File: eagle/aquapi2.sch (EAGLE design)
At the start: 5 parts, among them IC1 RASPBERRY_PI_ZERO_W__V1.3_

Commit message: schemtic added
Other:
- moved on the sheet: PH_PROBE
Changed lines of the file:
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@@
 </instance>
 <instance part="U$2" gate="G$1" x="200.66" y="48.26" smashed="yes"/>
-<instance part="PH_PROBE" gate="A" x="12.7" y="35.56" smashed="yes" rot="R90">
-<attribute name="NAME" x="6.985" y="29.21" size="1.778" layer="95" rot="R90"/>
-<attribute name="VALUE" x="20.32" y="29.21" size="1.778" layer="96" rot="R90"/>
+<instance part="PH_PROBE" gate="A" x="-12.7" y="40.64" smashed="yes" rot="R90">
+<attribute name="NAME" x="-18.415" y="34.29" size="1.778" layer="95" rot="R90"/>
+<attribute name="VALUE" x="-5.08" y="34.29" size="1.778" layer="96" rot="R90"/>
 </instance>
 <instance part="SUPPLY1" gate="GND" x="33.02" y="35.56" smashed="yes">
 <attribute name="VALUE" x="31.115" y="32.385" size="1.778" layer="96"/>
 </instance>
-<instance part="SUPPLY2" gate="GND" x="17.78" y="20.32" smashed="yes">
-<attribute name="VALUE" x="15.875" y="17.145" size="1.778" layer="96"/>
+<instance part="SUPPLY2" gate="GND" x="-7.62" y="25.4" smashed="yes">
+<attribute name="VALUE" x="-9.525" y="22.225" size="1.778" layer="96"/>
 </instance>
 <instance part="SUPPLY3" gate="GND" x="246.38" y="63.5" smashed="yes">
@@
 <attribute name="VALUE" x="168.275" y="55.245" size="1.778" layer="96"/>
 </instance>
-<instance part="SUPPLY6" gate="+5V" x="12.7" y="12.7" smashed="yes" rot="R180">
-<attribute name="VALUE" x="14.605" y="9.525" size="1.778" layer="96" rot="R180"/>
+<instance part="SUPPLY6" gate="+5V" x="-12.7" y="17.78" smashed="yes" rot="R180">
+<attribute name="VALUE" x="-10.795" y="14.605" size="1.778" layer="96" rot="R180"/>
 </instance>
 <instance part="SUPPLY7" gate="+5V" x="33.02" y="81.28" smashed="yes" rot="R180">
@@
 <attribute name="VALUE" x="31.115" y="47.625" size="1.778" layer="96"/>
 </instance>
-<instance part="U$3" gate="G$1" x="106.68" y="-71.12" smashed="yes"/>
-<instance part="SUPPLY14" gate="GND" x="93.98" y="-35.56" smashed="yes">
-<attribute name="VALUE" x="92.075" y="-38.735" size="1.778" layer="96"/>
+<instance part="U$3" gate="G$1" x="66.04" y="-55.88" smashed="yes"/>
+<instance part="SUPPLY14" gate="GND" x="53.34" y="-20.32" smashed="yes">
+<attribute name="VALUE" x="51.435" y="-23.495" size="1.778" layer="96"/>
 </instance>
-<instance part="SUPPLY15" gate="+5V" x="93.98" y="-20.32" smashed="yes" rot="R180">
-<attribute name="VALUE" x="95.885" y="-23.495" size="1.778" layer="96" rot="R180"/>
+<instance part="SUPPLY15" gate="+5V" x="53.34" y="-5.08" smashed="yes" rot="R180">
+<attribute name="VALUE" x="55.245" y="-8.255" size="1.778" layer="96" rot="R180"/>
 </instance>
 </instances>
@@
 <segment>
 <pinref part="PH_PROBE" gate="A" pin="1"/>
-<wire x1="10.16" y1="33.02" x2="10.16" y2="22.86" width="0.1524" layer="91"/>
-<junction x="10.16" y="22.86"/>
-<label x="7.62" y="22.86" size="1.778" layer="95" rot="R270"/>
+<wire x1="-15.24" y1="38.1" x2="-15.24" y2="27.94" width="0.1524" layer="91"/>
+<junction x="-15.24" y="27.94"/>
+<label x="-17.78" y="27.94" size="1.778" layer="95" rot="R270"/>
 </segment>
 <segment>
@@
 <segment>
 <pinref part="PH_PROBE" gate="A" pin="3"/>
-<wire x1="15.24" y1="33.02" x2="15.24" y2="22.86" width="0.1524" layer="91"/>
-<label x="17.78" y="22.86" size="1.778" layer="95"/>
-<junction x="15.24" y="22.86"/>
+<wire x1="-10.16" y1="38.1" x2="-10.16" y2="27.94" width="0.1524" layer="91"/>
+<label x="-7.62" y="27.94" size="1.778" layer="95"/>
+<junction x="-10.16" y="27.94"/>
 <pinref part="SUPPLY2" gate="GND" pin="GND"/>
-<wire x1="15.24" y1="22.86" x2="17.78" y2="22.86" width="0.1524" layer="91"/>
-<junction x="17.78" y="22.86"/>
+<wire x1="-10.16" y1="27.94" x2="-7.62" y2="27.94" width="0.1524" layer="91"/>
+<junction x="-7.62" y="27.94"/>
 </segment>
 <segment>
@@
 <segment>
 <pinref part="U$3" gate="G$1" pin="GND"/>
-<wire x1="95.25" y1="-30.48" x2="93.98" y2="-30.48" width="0.1524" layer="91"/>
+<wire x1="54.61" y1="-15.24" x2="53.34" y2="-15.24" width="0.1524" layer="91"/>
 <pinref part="SUPPLY14" gate="GND" pin="GND"/>
-<wire x1="93.98" y1="-30.48" x2="93.98" y2="-33.02" width="0.1524" layer="91"/>
+<wire x1="53.34" y1="-15.24" x2="53.34" y2="-17.78" width="0.1524" layer="91"/>
 </segment>
 </net>
@@
 <segment>
 <pinref part="PH_PROBE" gate="A" pin="2"/>
-<wire x1="12.7" y1="33.02" x2="12.7" y2="22.86" width="0.1524" layer="91"/>
-<junction x="12.7" y="22.86"/>
+<wire x1="-12.7" y1="38.1" x2="-12.7" y2="27.94" width="0.1524" layer="91"/>
+<junction x="-12.7" y="27.94"/>
 <pinref part="SUPPLY6" gate="+5V" pin="+5V"/>
-<wire x1="12.7" y1="22.86" x2="12.7" y2="15.24" width="0.1524" layer="91"/>
+<wire x1="-12.7" y1="27.94" x2="-12.7" y2="20.32" width="0.1524" layer="91"/>
 </segment>
 <segment>
@@
 <pinref part="U$3" gate="G$1" pin="VCC"/>
 <pinref part="SUPPLY15" gate="+5V" pin="+5V"/>
-<wire x1="95.25" y1="-15.24" x2="93.98" y2="-15.24" width="0.1524" layer="91"/>
-<wire x1="93.98" y1="-15.24" x2="93.98" y2="-17.78" width="0.1524" layer="91"/>
+<wire x1="54.61" y1="0" x2="53.34" y2="0" width="0.1524" layer="91"/>
+<wire x1="53.34" y1="0" x2="53.34" y2="-2.54" width="0.1524" layer="91"/>
 </segment>
 </net>

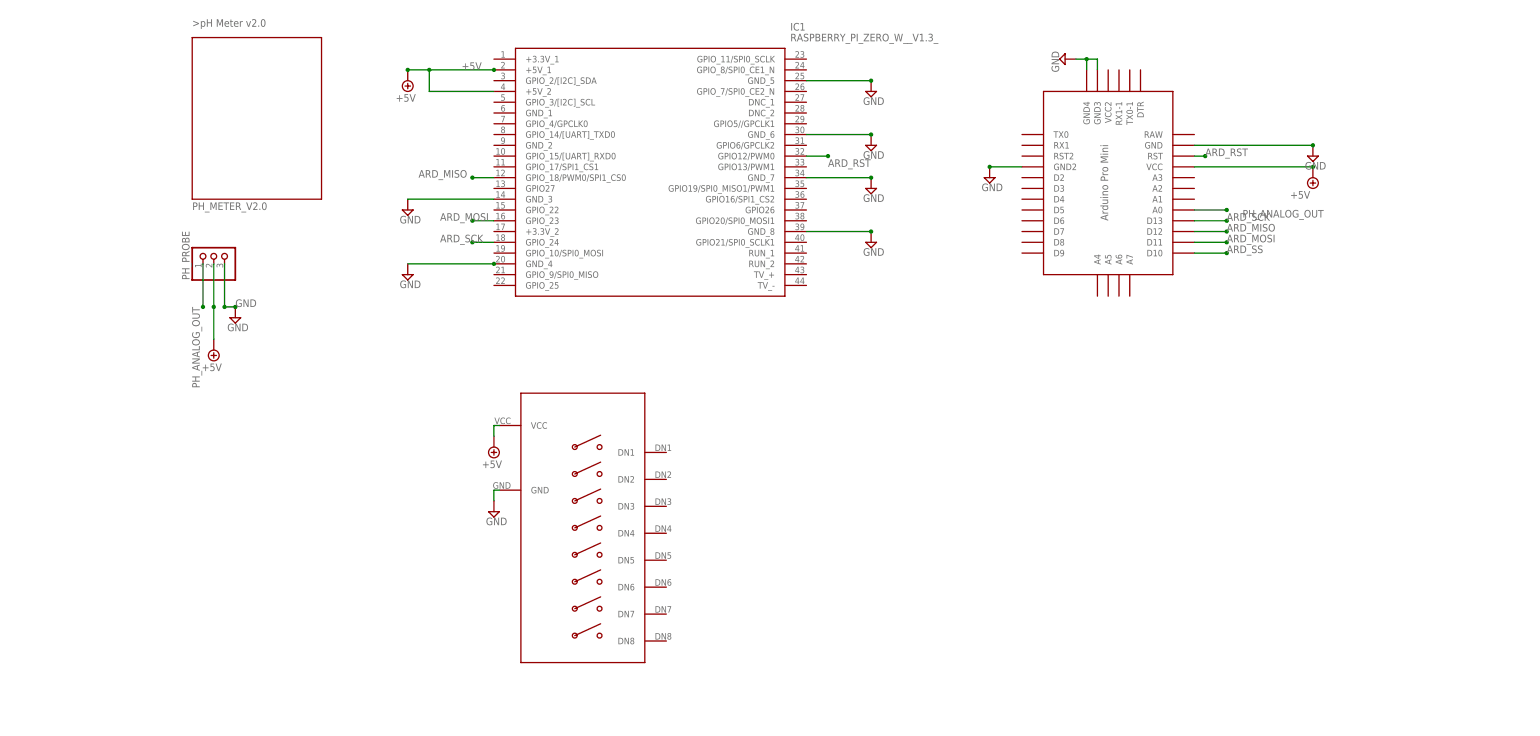
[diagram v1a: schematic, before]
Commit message: arudino device lib fixed
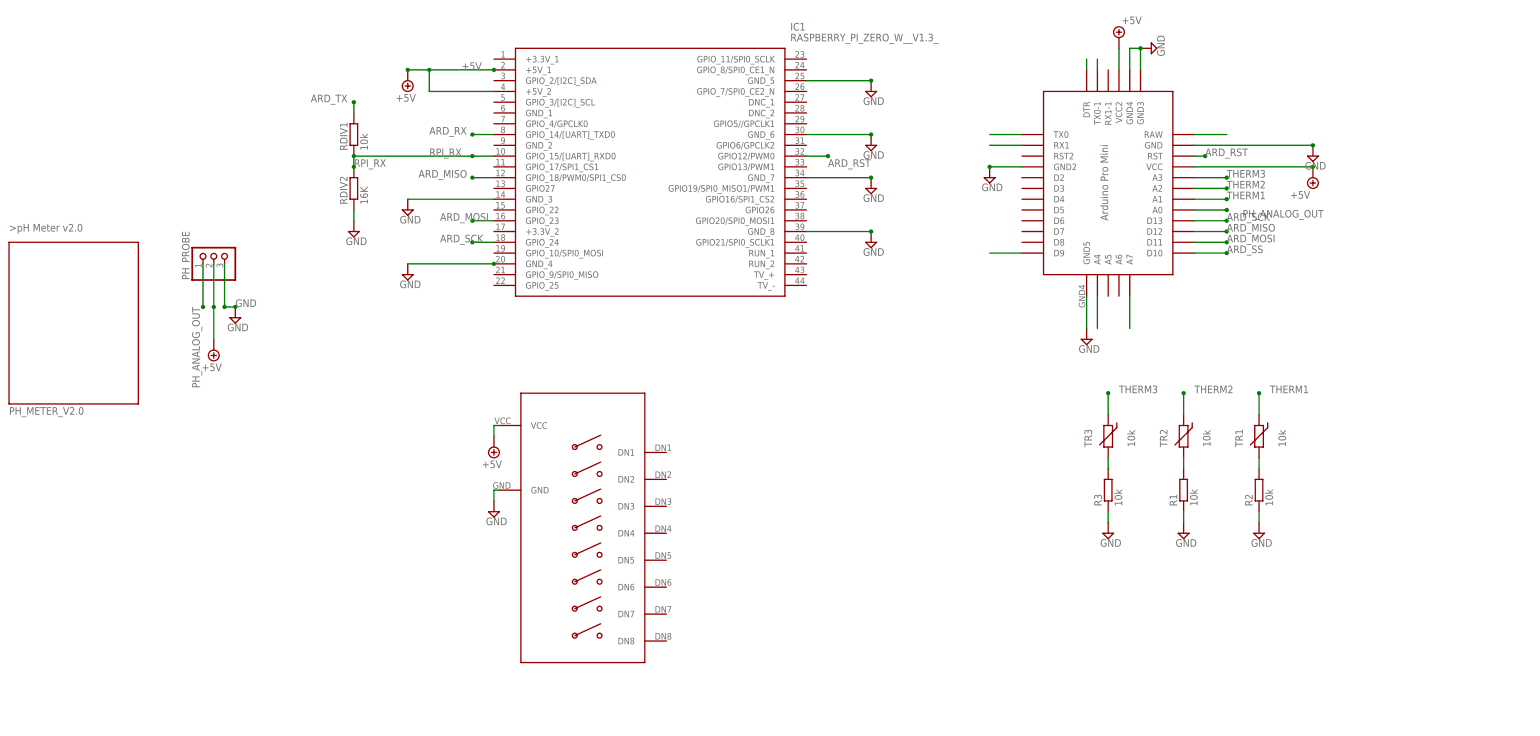
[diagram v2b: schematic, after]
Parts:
- added R1, R2, R3, RDIV1: 10k, rcl:R-EU_R0805
- added RDIV2: 16K, rcl:R-EU_R0805
- added TR1, TR2, TR3: 10k, discrete:THERMISTOR_R-2,5
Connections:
- new net ARD_RX: IC1.GPIO_14/[UART]_TXD0
- new net ARD_TX: RDIV1.2
- new net N$1: R2.2, TR1.2
- new net N$10: U$2.TX0-1
- new net N$13: U$2.GND
- new net N$14: U$2.GND5
- new net N$15: U$2.DTR
- new net N$2: R1.2, TR2.2
- new net N$3: R3.2, TR3.2
- new net N$4: U$2.RAW
- new net N$5: U$2.A7
- new net N$6: U$2.D9
- new net N$7: U$2.A4
- new net N$8: U$2.TX0
- new net N$9: U$2.RX1
- new net RPI_RX: IC1.GPIO_15/[UART]_RXD0, RDIV1.1, RDIV2.2
- new net THERM1: TR1.1, U$2.A1
- new net THERM2: TR2.1, U$2.A2
- new net THERM3: TR3.1, U$2.A3
- net +5V: now also U$2.VCC2
- net GND: now also R1.1, R2.1, R3.1, RDIV2.1; no longer U$2.GND

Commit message: Squashed commit of the following:
commit 7dce77e1b018337bae77b73dfeb2fe2afd6dd7fb
Author: rafal <ravmiecznk@gmail.com>
Date:   Mon Mar 27 18:15:28 2023 +0200

    new constructor from struct

commit 8f6d84a0210c76b2bc0acb519426c939a0a5c33f
Author: rafal <ravmiecznk@gmail.com>
Date:   Mon Mar 27 18:13:10 2023 +0200

    usart draft works

commit a12afc0a744ad612be8265cef467c83d1d3cefab
Author: rafal <ravmiecznk@gmail.com>
Date:   Mon Mar 27 17:49:51 2023 +0200

    schematic fix

commit a0211998f02243aec53f4161e691c0fde81374dd
Author: rafal <ravmiecznk@gmail.com>
Date:   Mon Mar 27 17:49:04 2023 +0200

    Usart constr added

commit c2ed277544ca2c68a412f2a85b5fd8a9273f73a5
Author: rafal <ravmiecznk@gmail.com>
Date:   Sun Mar 26 22:08:04 2023 +0200

    usart and circ buffer added

commit b830d1946cd96a0de6c5bb9a34da8aa961058b17
Author: rafal <ravmiecznk@gmail.com>
Date:   Sun Mar 26 19:27:24 2023 +0200

    avr cpp code added
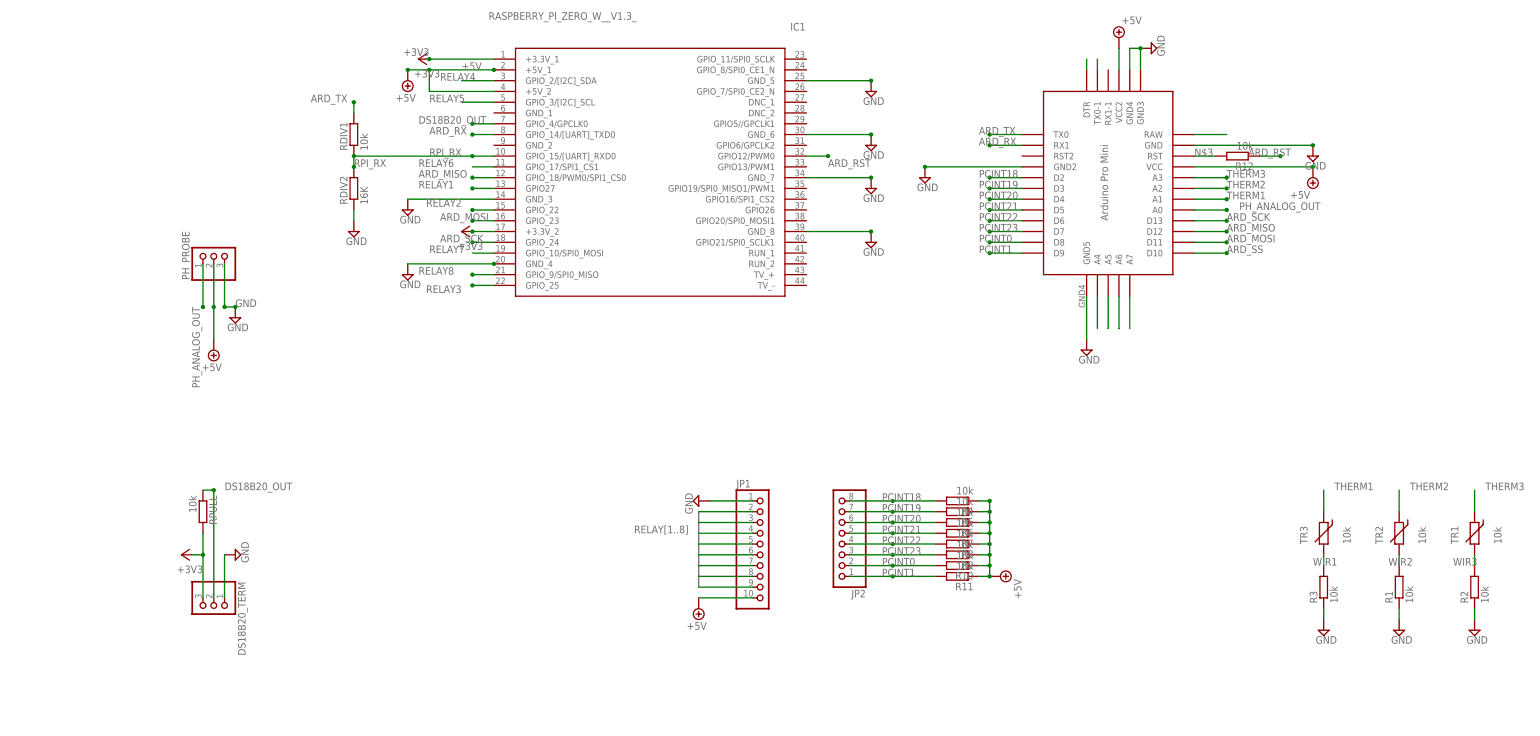
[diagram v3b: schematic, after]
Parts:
- removed U$1: PH_METER_V2.0, dforbot:PH_METER_V2.0
- removed U$3: RELAY_X8, RELAYx8:RELAY_X8
- added DS18B20_TERM: (no value), pinhead:PINHD-1X3
- added JP1: (no value), pinhead:PINHD-1X10
- added JP2: (no value), pinhead:PINHD-1X8
- added R10, R11, R12, R4, R5, R6, R7, R8, R9, RPULL: 10k, rcl:R-EU_R0805
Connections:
- net N$1 renamed WIR3
- net N$2 renamed WIR2
- net N$3 renamed WIR1
- removed net N$14: U$2.GND5
- removed net N$6: U$2.D9
- removed net N$8: U$2.TX0
- removed net N$9: U$2.RX1
- new net +3V3: DS18B20_TERM.3, IC1.+3.3V_1, IC1.+3.3V_2, RPULL.2
- new net DS18B20_OUT: DS18B20_TERM.2, IC1.GPIO_4/GPCLK0, RPULL.1
- new net N$1: U$2.A5
- new net N$2: U$2.A6
- new net N$3: R12.2, U$2.RST
- new net PCINT0: JP2.2, R10.2, U$2.D8
- new net PCINT1: JP2.1, R11.2, U$2.D9
- new net PCINT18: JP2.8, R4.2, U$2.D2
- new net PCINT19: JP2.7, R5.2, U$2.D3
- new net PCINT20: JP2.6, R6.2, U$2.D4
- new net PCINT21: JP2.5, R7.2, U$2.D5
- new net PCINT22: JP2.4, R8.2, U$2.D6
- new net PCINT23: JP2.3, R9.2, U$2.D7
- new net RELAY1: IC1.GPIO27, JP1.2
- new net RELAY2: IC1.GPIO_22, JP1.3
- new net RELAY3: IC1.GPIO_25, JP1.4
- new net RELAY4: IC1.GPIO_2/[I2C]_SDA, JP1.5
- new net RELAY5: IC1.GPIO_3/[I2C]_SCL, JP1.6
- new net RELAY6: IC1.GPIO_17/SPI1_CS1, JP1.7
- new net RELAY7: IC1.GPIO_10/SPI0_MOSI, JP1.8
- new net RELAY8: IC1.GPIO_9/SPI0_MISO, JP1.9
- net +5V: now also JP1.10, R10.1, R11.1, R4.1, R5.1, R6.1, R7.1, R8.1, R9.1; no longer U$3.VCC
- net ARD_RST: now also R12.1; no longer U$2.RST
- net ARD_RX: now also U$2.RX1
- net ARD_TX: now also U$2.TX0
- net GND: now also DS18B20_TERM.1, JP1.1, U$2.GND5; no longer U$3.GND
- net THERM1: now also TR3.1; no longer TR1.1
- net THERM3: now also TR1.1; no longer TR3.1
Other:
- moved on the sheet: R1, R2, R3, TR1, TR2, TR3
